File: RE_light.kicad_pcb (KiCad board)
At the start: 2 copper layers, 201.9 x 21.6 mm, 21 parts, among them J1 Conn_01x03_Female, J3 Conn_01x03_Female, U1 LM1117-3.3, U2 ESP-01v090

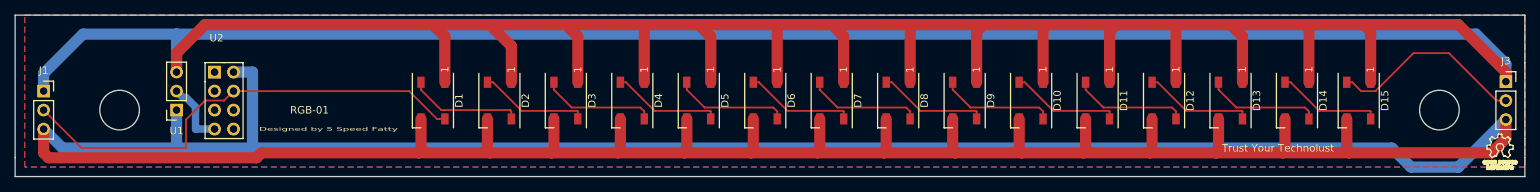
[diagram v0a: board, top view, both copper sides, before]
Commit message: adde silkscreens
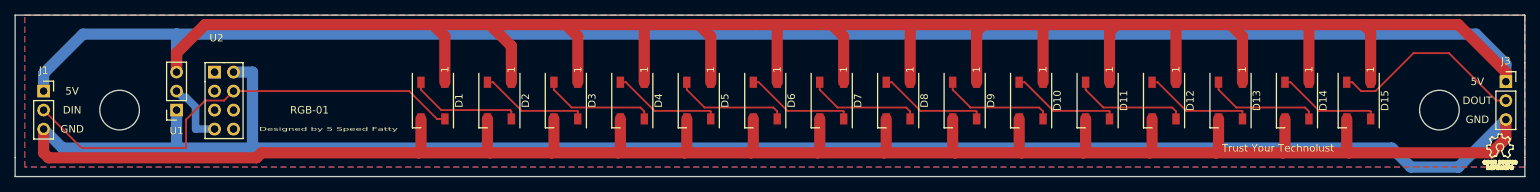
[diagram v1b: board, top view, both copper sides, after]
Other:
- board text added: "5V"
- board text added: "DIN"
- board text added: "DOUT"
- board text added: "GND"
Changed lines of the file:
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@@
   (general
     (thickness 1.6)
-    (drawings 1498)
+    (drawings 1504)
     (tracks 225)
     (zones 0)
@@
     )
   )
+  (gr_text GND (at 222.25 95.25) (layer F.SilkS)
+    (effects (font (size 1 1) (thickness 0.15)))
+  )
+  (gr_text DOUT (at 222.25 92.71) (layer F.SilkS)
+    (effects (font (size 1 1) (thickness 0.15)))
+  )
+  (gr_text "5V\n" (at 222.25 90.17) (layer F.SilkS)
+    (effects (font (size 1 1) (thickness 0.15)))
+  )
+  (gr_text GND (at 34.29 96.52) (layer F.SilkS)
+    (effects (font (size 1 1) (thickness 0.15)))
+  )
+  (gr_text DIN (at 34.29 93.98) (layer F.SilkS)
+    (effects (font (size 1 1) (thickness 0.15)))
+  )
+  (gr_text 5V (at 34.29 91.44) (layer F.SilkS)
+    (effects (font (size 1 1) (thickness 0.15)))
+  )
   (gr_text "Designed by 5 Speed Fatty" (at 68.58 96.52) (layer F.SilkS)
